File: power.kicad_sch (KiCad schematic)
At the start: 26 parts, among them J1 USB_C_Receptacle_USB2.0_14P, U2 nPM1300-QEXX

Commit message: add inductor and crystal
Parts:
- L1, L2: footprint (none) -> Library:L0806; Model (none) -> MLP2016H2R2MT0S1
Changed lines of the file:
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@@
 			)
 		)
-		(property "Footprint" ""
+		(property "Footprint" "Library:L0806"
 			(at 151.13 119.38 0)
 			(effects
@@
 			)
 		)
+		(property "Model" "MLP2016H2R2MT0S1"
+			(at 151.13 119.38 0)
+			(effects
+				(font
+					(size 1.27 1.27)
+				)
+				(hide yes)
+			)
+		)
 		(pin "1"
 		)
@@
 			)
 		)
-		(property "Footprint" ""
+		(property "Footprint" "Library:L0806"
 			(at 151.13 106.68 0)
 			(effects
@@
 			(at 151.13 106.68 0)
 			(effects
+				(font
+					(size 1.27 1.27)
+				)
+				(hide yes)
+			)
+		)
+		(property "Model" "MLP2016H2R2MT0S1"
+			(at 151.13 106.68 0)
+			(effects

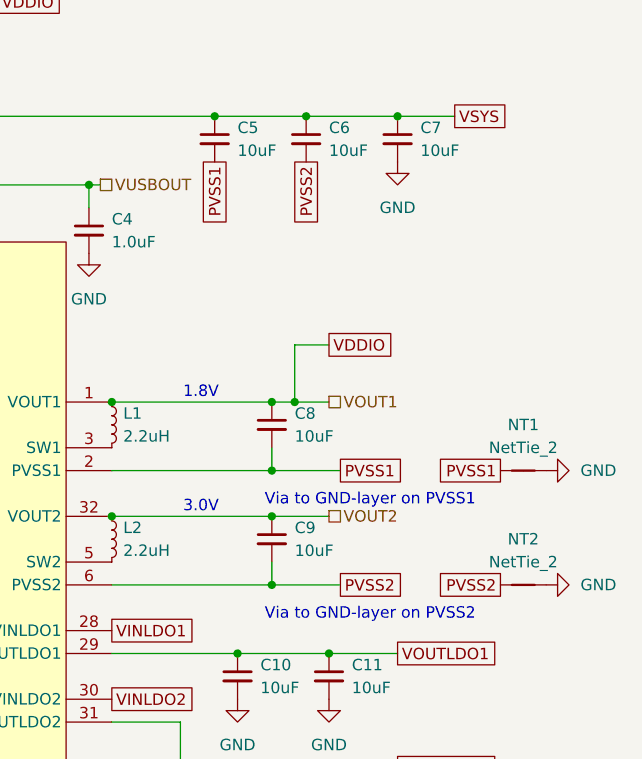
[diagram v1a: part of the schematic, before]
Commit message: fixup design pcb clearances
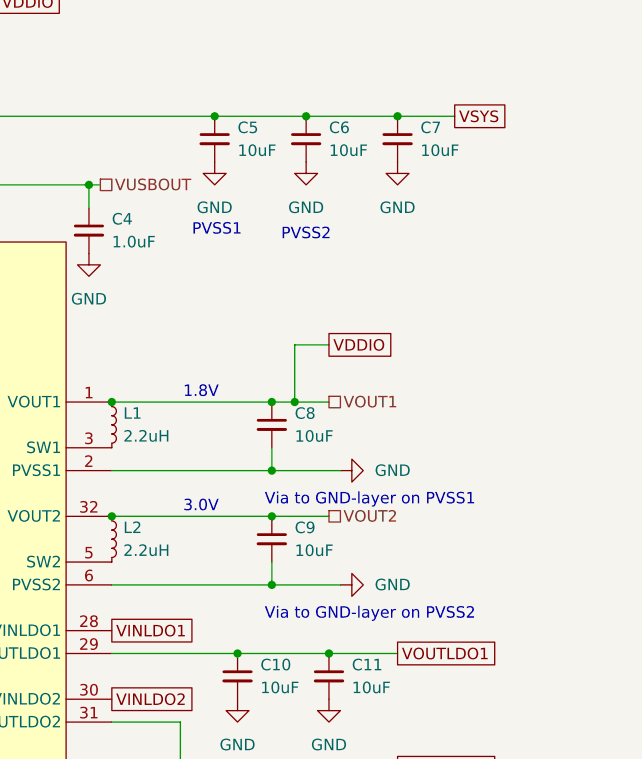
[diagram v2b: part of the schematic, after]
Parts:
- removed NT1, NT2: NetTie_2, symbol Device:NetTie_2
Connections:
- net PVSS1 is gone; now on net GND: C5.2, C8.2, U2.2 (PVSS1)
- net PVSS2 is gone; now on net GND: C6.2, C9.2, U2.6 (PVSS2)
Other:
- note added: "PVSS1"
- note added: "PVSS2"

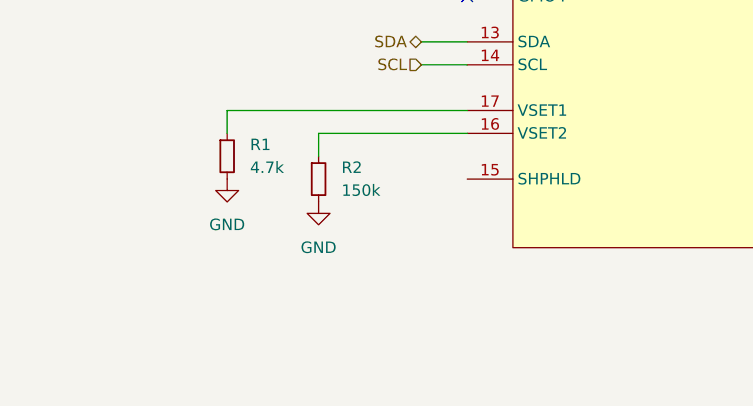
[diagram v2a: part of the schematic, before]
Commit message: add power button
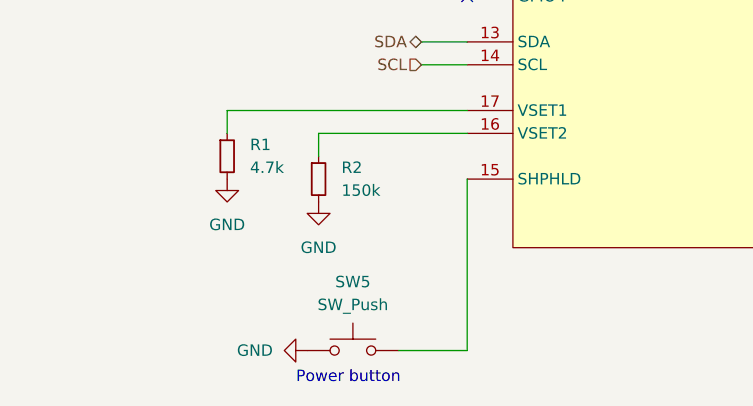
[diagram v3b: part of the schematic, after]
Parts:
- added SW5: SW_Push, symbol Switch:SW_Push
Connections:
- net GND: now also SW5.1
- net at U2.15 (SHPHLD): now also SW5.2
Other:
- note added: "Power button"
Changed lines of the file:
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@@
+	(wire
+		(pts
+			(xy 80.01 149.86) (xy 80.01 168.91)
+		)
+		(stroke
+			(width 0)
+			(type default)
+		)
+	)
 	(wire
 		(pts
@@
 	(wire
 		(pts
+			(xy 80.01 168.91) (xy 72.39 168.91)
+		)
+		(stroke
+			(width 0)
+			(type default)
+		)
+	)
+	(wire
+		(pts
 			(xy 50.8 97.79) (xy 50.8 101.6)
 		)
@@
 		(exclude_from_sim no)
 		(at 179.832 127.762 0)
+		(effects
+			(font
+				(size 1.27 1.27)
+			)
+		)
+	)
+	(text "Power button"
+		(exclude_from_sim no)
+		(at 66.802 171.958 0)
 		(effects
 			(font
@@
 	)
 	(symbol
+		(lib_id "power:GND")
+		(at 62.23 168.91 270)
+		(unit 1)
+		(exclude_from_sim no)
+		(in_bom yes)
+		(on_board yes)
+		(dnp no)
+		(fields_autoplaced yes)
+		(property "Reference" "#PWR062"
+			(at 55.88 168.91 0)
+			(effects
+				(font
+					(size 1.27 1.27)
+				)
+				(hide yes)
+			)
+		)
+		(property "Value" "GND"
+			(at 58.42 168.9099 90)
+			(effects
+				(font
+					(size 1.27 1.27)
+				)
+				(justify right)
+			)
+		)
+		(property "Footprint" ""
+			(at 62.23 168.91 0)
+			(effects
+				(font
+					(size 1.27 1.27)
+				)
+				(hide yes)
+			)
+		)
+		(property "Datasheet" ""
+			(at 62.23 168.91 0)
+			(effects
+				(font
+					(size 1.27 1.27)
+				)
+				(hide yes)
+			)
+		)
+		(property "Description" "Power symbol creates a global label with name \"GND\" , ground"
+			(at 62.23 168.91 0)
+			(effects
+				(font
+					(size 1.27 1.27)
+				)
+				(hide yes)
+			)
+		)
+		(pin "1"
+		)
+		(instances
+			(project "OpenBikeComputer"
+				(path "/110ea5a2-03d6-426d-b79f-fcb4ea6cee9d/37638529-c791-4545-86be-d41ede14aac5"
+					(reference "#PWR062")
+					(unit 1)
+				)
+			)
+		)
+	)
+	(symbol
 		(lib_id "Device:C_Small")
 		(at 182.88 74.93 0)
@@
 					(unit 1)
 				)
+			)
+		)
+	)
+	(symbol
+		(lib_id "Switch:SW_Push")
+		(at 67.31 168.91 0)
+		(unit 1)
+		(exclude_from_sim no)
+		(in_bom yes)
+		(on_board yes)
+		(dnp no)
+		(fields_autoplaced yes)
+		(property "Reference" "SW5"
+			(at 67.31 161.29 0)
+			(effects
+				(font
+					(size 1.27 1.27)
+				)
+			)
+		)
+		(property "Value" "SW_Push"
+			(at 67.31 163.83 0)
+			(effects
+				(font
+					(size 1.27 1.27)
+				)
+			)
+		)
+		(property "Footprint" ""
+			(at 67.31 163.83 0)
+			(effects
+				(font
+					(size 1.27 1.27)
+				)
+				(hide yes)
+			)
+		)
+		(property "Datasheet" "~"
+			(at 67.31 163.83 0)
+			(effects
+				(font
+					(size 1.27 1.27)
+				)
+				(hide yes)
+			)
+		)
+		(property "Description" "Push button switch, generic, two pins"
+			(at 67.31 168.91 0)
+			(effects
+				(font
+					(size 1.27 1.27)
+				)
+				(hide yes)
+			)
+		)
+		(pin "2"
+		)
+		(pin "1"
+		)
+		(instances
+			(project "OpenBikeComputer"
+				(path "/110ea5a2-03d6-426d-b79f-fcb4ea6cee9d/37638529-c791-4545-86be-d41ede14aac5"
+					(reference "SW5")
+					(unit 1)
+				)

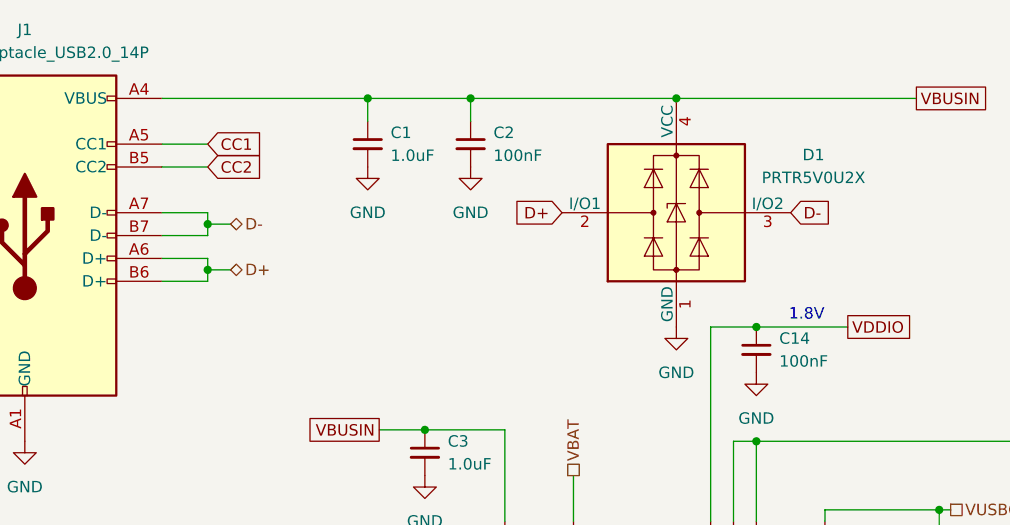
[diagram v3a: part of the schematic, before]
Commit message: switch out SoC, stuff is in the air
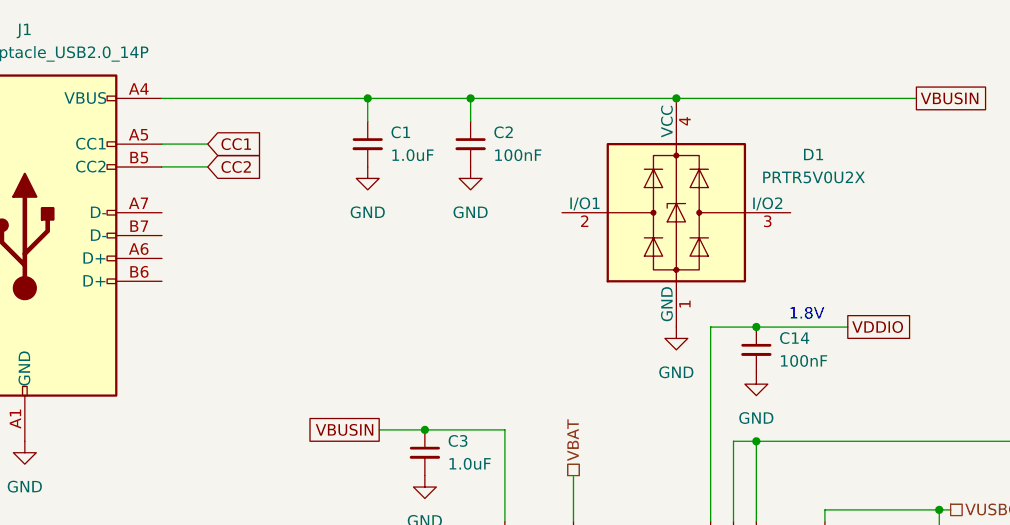
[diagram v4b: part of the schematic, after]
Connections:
- removed net D+: D1.2 (I/O1), J1.A6 (D+), J1.B6 (D+)
- removed net D-: D1.3 (I/O2), J1.A7 (D-), J1.B7 (D-)
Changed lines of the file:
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@@
-	)
-	(junction
-		(at 67.31 53.34)
-		(diameter 0)
-		(color 0 0 0 0)
 	)
 	(junction
@@
 	(junction
 		(at 151.13 104.14)
-		(diameter 0)
-		(color 0 0 0 0)
-	)
-	(junction
-		(at 67.31 48.26)
 		(diameter 0)
 		(color 0 0 0 0)
@@
 	(wire
 		(pts
-			(xy 62.23 46.99) (xy 67.31 46.99)
-		)
-		(stroke
-			(width 0)
-			(type default)
-		)
-	)
-	(wire
-		(pts
 			(xy 151.13 132.08) (xy 165.1 132.08)
 		)
@@
 	(wire
 		(pts
-			(xy 62.23 52.07) (xy 67.31 52.07)
-		)
-		(stroke
-			(width 0)
-			(type default)
-		)
-	)
-	(wire
-		(pts
 			(xy 158.75 144.78) (xy 165.1 144.78)
 		)
@@
 	(wire
 		(pts
-			(xy 62.23 49.53) (xy 67.31 49.53)
-		)
-		(stroke
-			(width 0)
-			(type default)
-		)
-	)
-	(wire
-		(pts
 			(xy 175.26 132.08) (xy 182.88 132.08)
 		)
@@
 	(wire
 		(pts
-			(xy 67.31 46.99) (xy 67.31 48.26)
-		)
-		(stroke
-			(width 0)
-			(type default)
-		)
-	)
-	(wire
-		(pts
 			(xy 63.5 144.78) (xy 63.5 147.32)
 		)
@@
 	(wire
 		(pts
-			(xy 67.31 53.34) (xy 69.85 53.34)
-		)
-		(stroke
-			(width 0)
-			(type default)
-		)
-	)
-	(wire
-		(pts
 			(xy 168.91 109.22) (xy 168.91 111.76)
 		)
@@
 	(wire
 		(pts
-			(xy 67.31 48.26) (xy 69.85 48.26)
-		)
-		(stroke
-			(width 0)
-			(type default)
-		)
-	)
-	(wire
-		(pts
 			(xy 165.1 132.08) (xy 175.26 132.08)
 		)
@@
 	(wire
 		(pts
-			(xy 67.31 52.07) (xy 67.31 53.34)
-		)
-		(stroke
-			(width 0)
-			(type default)
-		)
-	)
-	(wire
-		(pts
 			(xy 175.26 144.78) (xy 182.88 144.78)
 		)
@@
 	(wire
 		(pts
-			(xy 62.23 54.61) (xy 67.31 54.61)
-		)
-		(stroke
-			(width 0)
-			(type default)
-		)
-	)
-	(wire
-		(pts
 			(xy 151.13 111.76) (xy 168.91 111.76)
 		)
@@
 	(wire
 		(pts
-			(xy 67.31 48.26) (xy 67.31 49.53)
-		)
-		(stroke
-			(width 0)
-			(type default)
-		)
-	)
-	(wire
-		(pts
 			(xy 151.13 116.84) (xy 168.91 116.84)
 		)
@@
 		(pts
 			(xy 62.23 41.91) (xy 67.31 41.91)
-		)
-		(stroke
-			(width 0)
-			(type default)
-		)
-	)
-	(wire
-		(pts
-			(xy 67.31 53.34) (xy 67.31 54.61)
 		)
 		(stroke
@@
 		)
 	)
-	(global_label "D+"
-		(shape input)
-		(at 106.68 46.99 180)
-		(fields_autoplaced yes)
-		(effects
-			(font
-				(size 1.27 1.27)
-			)
-			(justify right)
-		)
-		(property "Intersheetrefs" "${INTERSHEET_REFS}"
-			(at 100.8524 46.99 0)
-			(effects
-				(font
-					(size 1.27 1.27)
-				)
-				(justify right)
-				(hide yes)
-			)
-		)
-	)
 	(global_label "CC1"
 		(shape input)
@@
 		)
 	)
-	(global_label "D-"
-		(shape input)
-		(at 132.08 46.99 0)
-		(fields_autoplaced yes)
-		(effects
-			(font
-				(size 1.27 1.27)
-			)
-			(justify left)
-		)
-		(property "Intersheetrefs" "${INTERSHEET_REFS}"
-			(at 137.9076 46.99 0)
-			(effects
-				(font
-					(size 1.27 1.27)
-				)
-				(justify left)
-				(hide yes)
-			)
-		)
-	)
 	(global_label "VSYS"
 		(shape passive)
@@
 		)
 	)
-	(hierarchical_label "D-"
-		(shape bidirectional)
-		(at 69.85 48.26 0)
-		(fields_autoplaced yes)
-		(effects
-			(font
-				(size 1.27 1.27)
-			)
-			(justify left)
-		)
-	)
 	(hierarchical_label "SCL"
 		(shape input)
@@
 		(fields_autoplaced yes)
 		(effects
-			(font
-				(size 1.27 1.27)
-			)
-			(justify left)
-		)
-	)
-	(hierarchical_label "D+"
-		(shape bidirectional)
-		(at 69.85 53.34 0)
-		(fields_autoplaced yes)
-		(effects

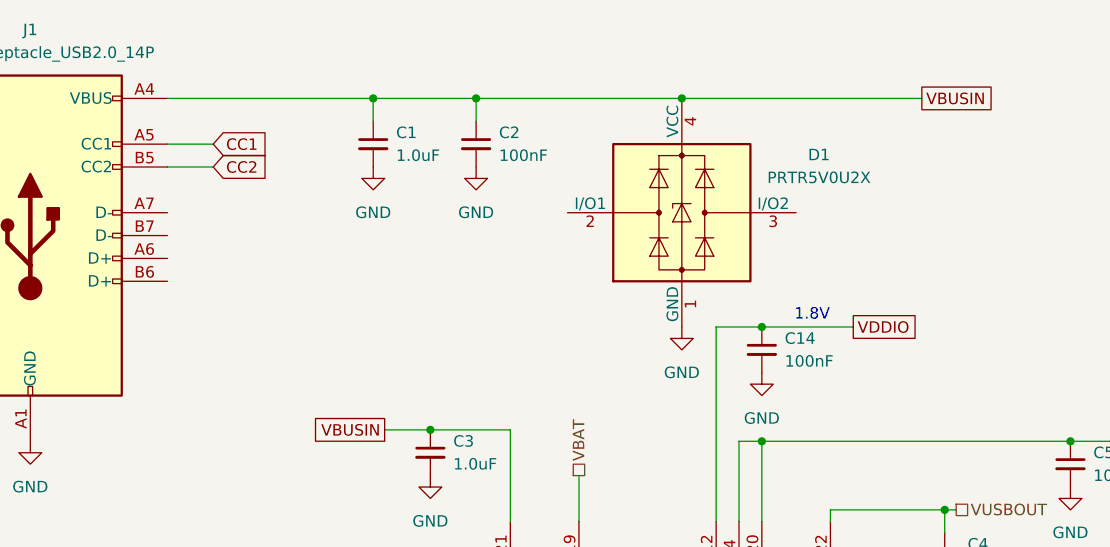
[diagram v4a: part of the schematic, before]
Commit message: re-integrate all components + add BT antenna
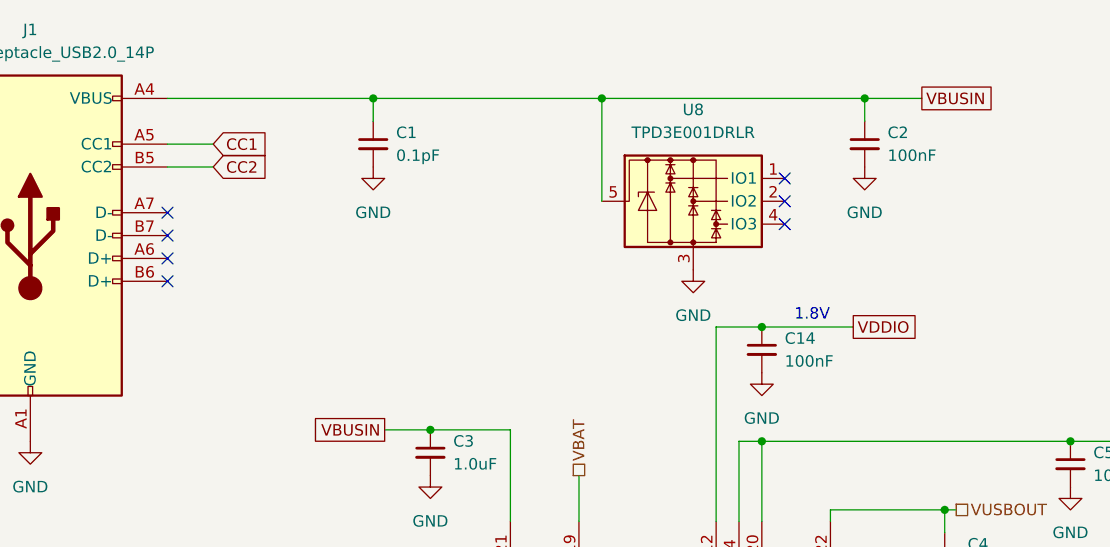
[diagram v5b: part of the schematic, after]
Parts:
- removed D1: PRTR5V0U2X, Package_TO_SOT_SMD:SOT-143, symbol Power_Protection:PRTR5V0U2X
- added U8: TPD3E001DRLR, Package_TO_SOT_SMD:SOT-553, symbol Power_Protection:TPD3E001DRLR
- C1: value 1.0uF -> 0.1pF
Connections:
- net GND: now also U8.3
- net VBUSIN: now also U8.5
- no-connect marks 3 -> 10

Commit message: rfinish routing PMIC (pretty crap routing)
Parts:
- C4: now not fitted
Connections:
- net VUSBOUT: no longer names the net of C4.1, U2.22 (VBUSOUT)
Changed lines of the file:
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@@
-	)
-	(junction
-		(at 148.59 80.01)
-		(diameter 0)
-		(color 0 0 0 0)
 	)
 	(junction
@@
 	(wire
 		(pts
-			(xy 148.59 80.01) (xy 149.86 80.01)
-		)
-		(stroke
-			(width 0)
-			(type default)
-		)
-	)
-	(wire
-		(pts
 			(xy 125.73 72.39) (xy 128.27 72.39)
 		)
@@
 		(shape passive)
 		(at 175.26 104.14 0)
-		(fields_autoplaced yes)
-		(effects
-			(font
-				(size 1.27 1.27)
-			)
-			(justify left)
-		)
-	)
-	(hierarchical_label "VUSBOUT"
-		(shape passive)
-		(at 149.86 80.01 0)
 		(fields_autoplaced yes)
 		(effects
@@
 		(exclude_from_sim no)
 		(in_bom yes)
-		(on_board yes)
-		(dnp no)
+		(on_board no)
+		(dnp yes)
 		(fields_autoplaced yes)
 		(property "Reference" "#PWR09"
@@
 		(exclude_from_sim no)
 		(in_bom yes)
-		(on_board yes)
-		(dnp no)
+		(on_board no)
+		(dnp yes)
 		(fields_autoplaced yes)
 		(property "Reference" "C4"

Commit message: shitty routing job for rev1
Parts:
- C10, C11, C12, C13: footprint Capacitor_SMD:C_0402_1005Metric -> (none); now not fitted

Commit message: add lots of test points
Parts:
- added TP1, TP2, TP5, TP6: TestPoint, symbol Connector:TestPoint
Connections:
- net INT: now also TP6.1
- net RESET: now also TP5.1
- net VDDIO: now also TP1.1
- net VOUT2: now also TP2.1
